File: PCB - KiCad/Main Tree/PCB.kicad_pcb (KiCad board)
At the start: 2 copper layers, 100 x 99.8 mm, 44 parts, among them J1 Secondary Tree 1, J2 Secondary Tree 2, J3 USB_B_Micro, J4 BATT, U1 LM555, U2 ULN2003, U3 4017

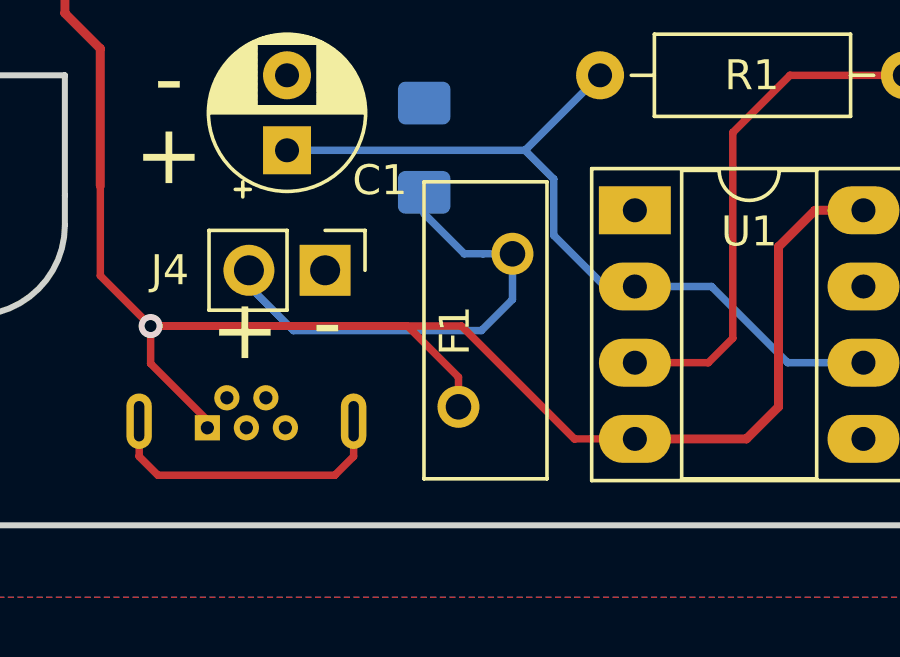
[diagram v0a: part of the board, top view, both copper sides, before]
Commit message: Some drawing and part changes
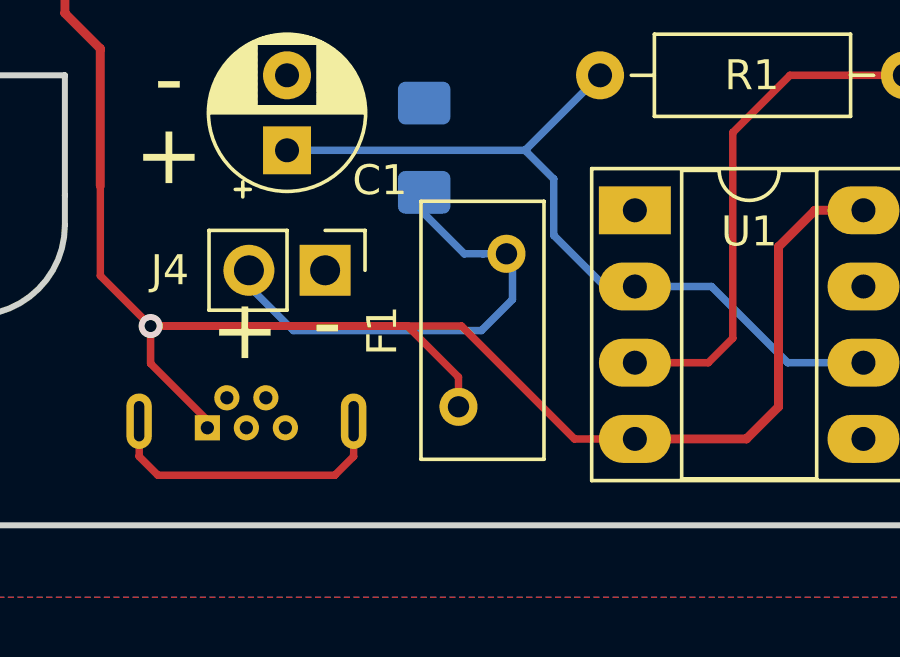
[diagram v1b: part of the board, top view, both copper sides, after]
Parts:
- F1: footprint Fuse:Fuse_BelFuse_0ZRE0025FF_L9.6mm_W3.8mm -> Fuse:Fuse_BelFuse_0ZRE0005FF_L8.3mm_W3.8mm
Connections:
- J3 pad 2: Net-(J3-Pad2) -> (no net)
- J3 pad 3: Net-(J3-Pad3) -> (no net)
- J3 pad 4: Net-(J3-Pad4) -> (no net)
- U1 pad 5: Net-(U1-Pad5) -> (no net)
- U1 pad 7: Net-(U1-Pad7) -> (no net)
- U3 pad 11: Net-(U3-Pad11) -> (no net)
- U3 pad 12: Net-(U3-Pad12) -> (no net)
- U3 pad 9: Net-(U3-Pad9) -> (no net)
